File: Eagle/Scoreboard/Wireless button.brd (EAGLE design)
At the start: 78.4 x 48.2 mm, 30 parts, among them Q1 2N3904, Q2 IRF9530

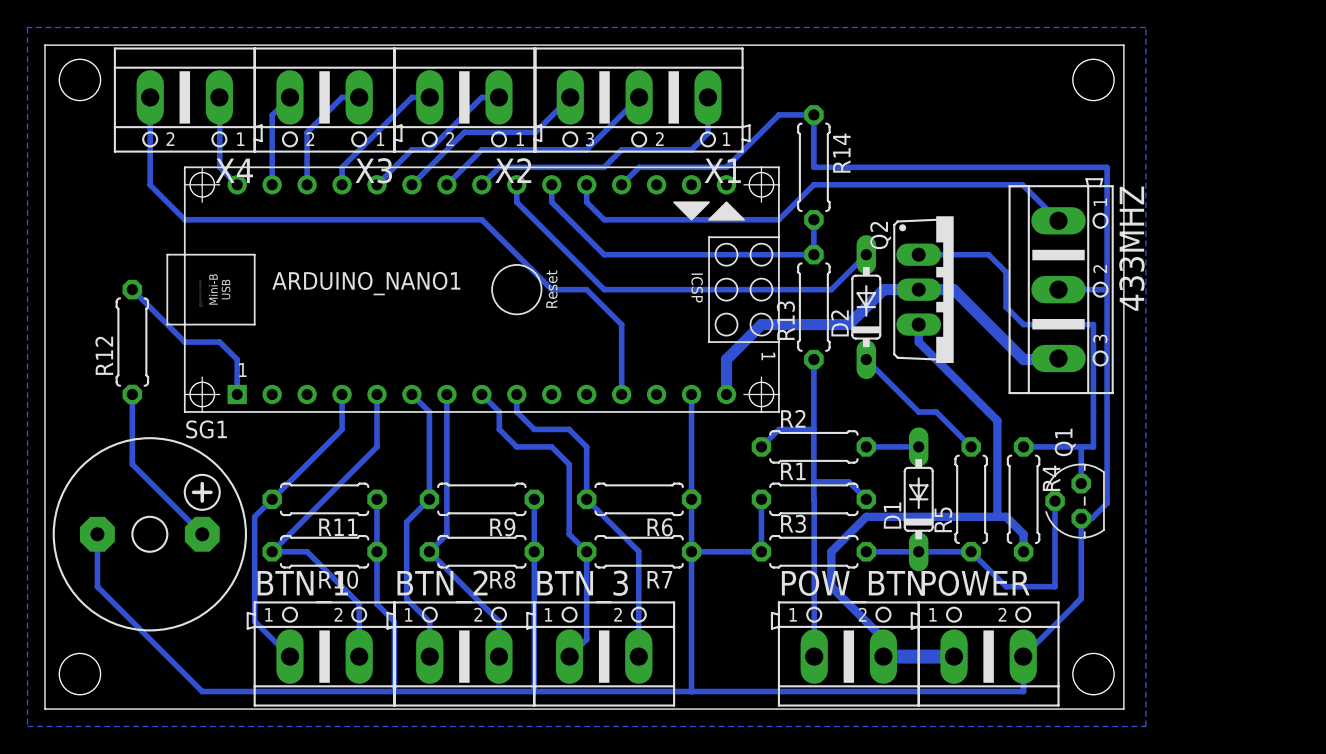
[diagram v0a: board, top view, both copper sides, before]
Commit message: Power for 433Mhz transmitter taking from 5V
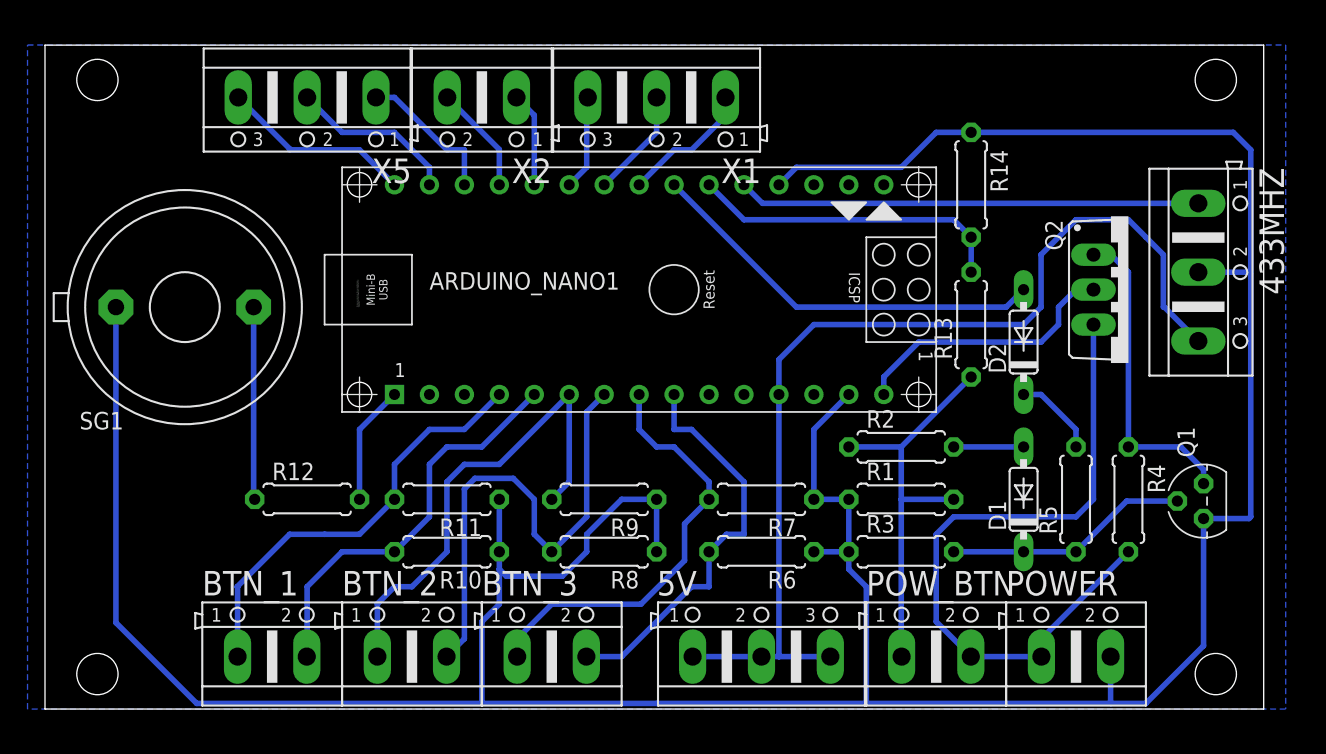
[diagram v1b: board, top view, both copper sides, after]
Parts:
- removed X3, X4: (no value), con-ptr500:AK500/2
- added 5V, X5: (no value), con-ptr500:AK500/3
- R10, R11, R6, R7, R8, R9: value (none) -> 10k
- SG1: value F/CM12P -> F/EE17P; device buzzer:F/CM12P -> buzzer:F/EE17P
- moved R12 17.1 mm to (19.1, 15.2), turned to 0 degrees
- moved SG1 16.7 mm to (10.2, 29.2), turned to 180 degrees
- moved Q2 12.7 mm to (78.7, 30.5)
- moved D2 11.7 mm to (71.1, 26.7)
- moved R13 11.5 mm to (67.3, 27.9)
- moved R14 11.5 mm to (67.3, 38.1)
- moved ARDUINO_NANO1 11.4 mm to (45.7, 30.5)
- moved 433MHZ 10.2 mm to (83.8, 31.8)
- moved R6 9.67 mm to (52.1, 11.4)
- moved R7 9.67 mm to (52.1, 15.2)
- moved R10 8.89 mm to (29.2, 11.4)
- moved R11 8.89 mm to (29.2, 15.2)
- moved R8 8.89 mm to (40.6, 11.4)
- moved R9 8.89 mm to (40.6, 15.2)
- moved Q1 8.89 mm to (84.2, 15.1)
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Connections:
- net 433_IN renamed N$10
- net N$10 renamed AWAY_UP
- net N$11 renamed AWAY_DOWN
- net N$12 renamed HOME_UP
- net N$13 renamed HOME_DOWN
- net N$14 renamed SWAP
- net N$16 renamed RESET
- net 5V: now also 433MHZ.3, 5V.1, 5V.2, 5V.3; no longer X4.2
- net GND: now also SG1.2; no longer SG1.-
- net N$18: now also X5.1; no longer X3.1
- net N$19: now also X5.2; no longer X3.2
- net N$20: now also X5.3; no longer X4.1
- net N$9: now also SG1.1; no longer SG1.+
- net VCC: no longer 433MHZ.3
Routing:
- net GND: track 219.6 -> 252.2 mm
- net 5V: track 49.9 -> 74.4 mm
- net HOME_DOWN: track 21.7 -> 36.1 mm
- net HOME_UP: track 21.0 -> 35.2 mm
- net VCC: track 30.9 -> 19.9 mm
- net N$3: track 20.6 -> 9.76 mm
- net N$2: track 32.9 -> 22.9 mm
- net AWAY_UP: track 22.7 -> 31.4 mm
- net N$7: track 16.6 -> 7.93 mm
- net SWAP: track 24.2 -> 31.5 mm
- net N$8: track 14.1 -> 6.91 mm
- net N$20: track 6.90 -> 14.0 mm
- net RESET: track 24.2 -> 29.6 mm
- net N$19: track 6.89 -> 12.3 mm
- net N$10: track 38.2 -> 33.6 mm
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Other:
- board size 78.4 x 48.2 mm -> 88.6 x 48.2 mm
